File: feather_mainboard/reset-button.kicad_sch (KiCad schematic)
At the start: 4 parts

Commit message: changed footprints location to match the new folder. TODO: check if the path is working on another computer
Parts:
- C10: footprint footprints:WCAP-CSGP_1210_H2.0 -> Custom footprints:WCAP-CSGP_1210_H2.0
- S5: footprint footprints:430182050816 -> Custom footprints:430182050816
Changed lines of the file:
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@@
 			)
 		)
-		(property "Footprint" "footprints:WCAP-CSGP_1210_H2.0"
+		(property "Footprint" "Custom footprints:WCAP-CSGP_1210_H2.0"
 			(at 125.73 106.68 0)
 			(effects
@@
 			)
 		)
-		(property "Footprint" "footprints:430182050816"
+		(property "Footprint" "Custom footprints:430182050816"
 			(at 147.32 106.68 0)
 			(effects

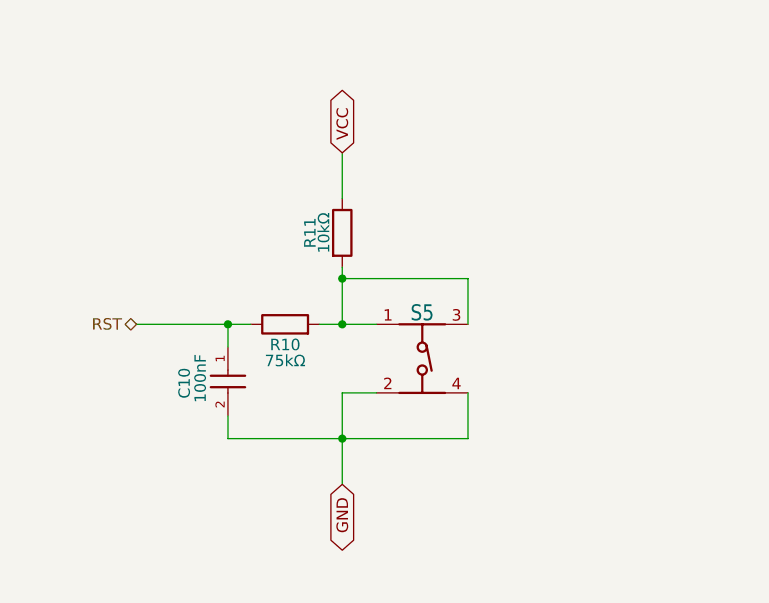
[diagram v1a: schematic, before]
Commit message: added daughter board
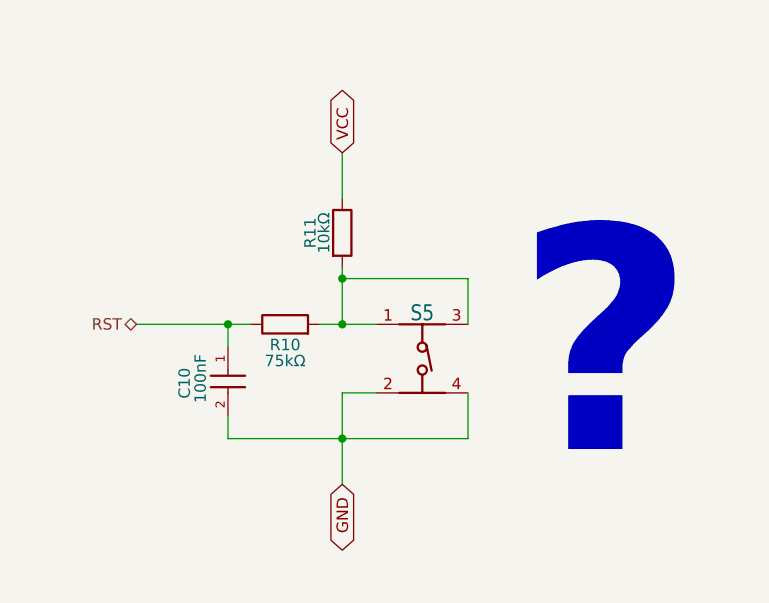
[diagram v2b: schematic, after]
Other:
- note added: "?"
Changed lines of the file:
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@@
+		)
+	)
+	(text "?"
+		(exclude_from_sim no)
+		(at 167.64 104.14 0)
+		(effects
+			(font
+				(size 25 25)
+				(thickness 5)
+				(bold yes)
+			)
 		)
 	)

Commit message: finished mainboard design, need to do the routing
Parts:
- removed C10: 100nF, Custom footprints:WCAP-CSGP_1210_H2.0, symbol WCAP-CSGP_1210_H2.0:WCAP-CSGP_1210_H2.0
- removed R10: 75kΩ, Resistor_SMD:R_0805_2012Metric_Pad1.20x1.40mm_HandSolder, symbol Device:R
- removed R11: 10kΩ, Resistor_SMD:R_0805_2012Metric_Pad1.20x1.40mm_HandSolder, symbol Device:R
- removed S5: 430182050816, Custom footprints:430182050816, symbol Projektarbeit_button:430182050816
- added C1_3: 100nF, Custom footprints:WCAP-CSGP_0603_R, symbol WCAP-CSGP_0603:WCAP-CSGP_0603
- added J3: 61300211121, Custom footprints:61300211121, symbol 6130XX11121_61300211121:6130XX11121_61300211121
- added R1_5: 10kΩ, Custom footprints:WRIS-RSKS_0603_REFLOW, symbol WRIS-RSKS_0603:WRIS-RSKS_0603
- added R3_1: 75kΩ, Custom footprints:WRIS-RSKS_0603_REFLOW, symbol WRIS-RSKS_0603:WRIS-RSKS_0603
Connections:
- net GND: now also C1_3.2, J3.2
- net RST: now also C1_3.1, R3_1.1
- net VCC: now also R1_5.2
- new net: J3.1, R1_5.1, R3_1.2
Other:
- note removed: "?"

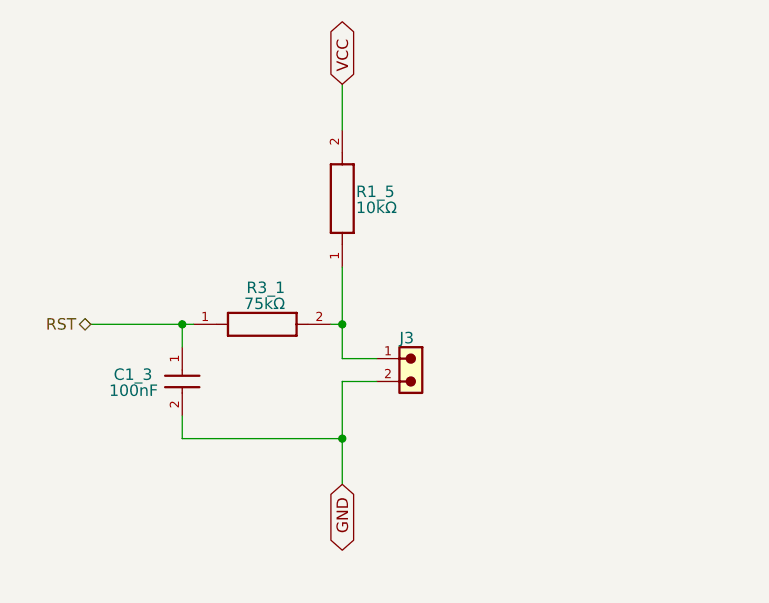
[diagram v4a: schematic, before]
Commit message: Updated the mainboard: removed unnecessary pull-ups on SD card lines; connected IIC pull-ups to enable circuit; cleaned up schematic
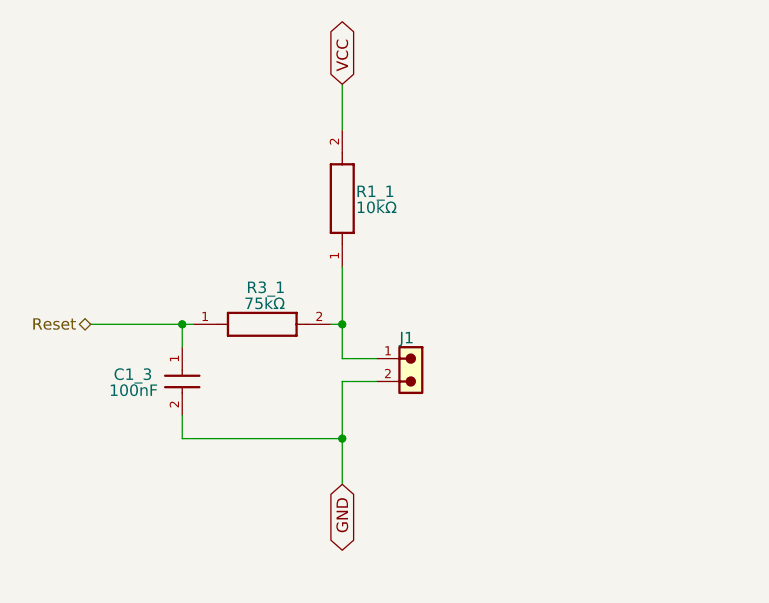
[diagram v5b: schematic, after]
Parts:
- renumbered J3 to J1, R1_5 to R1_1
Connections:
- net RST renamed Reset
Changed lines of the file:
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@@
 		)
 	)
-	(hierarchical_label "RST"
+	(hierarchical_label "Reset"
 		(shape bidirectional)
 		(at 110.49 101.6 180)
+		(fields_autoplaced yes)
 		(effects
 			(font
@@
 		(instances
 			(project "feather_mainboard"
-				(path "/e1e12730-ab4f-45db-8b66-c1e0f78e2f00/0d3ffa4d-b734-4a21-ae0e-364ca9762bbd"
+				(path "/e1e12730-ab4f-45db-8b66-c1e0f78e2f00/05fa08fc-e98a-44c0-b5db-55a9f347530b"
 					(reference "C1_3")
 					(unit 1)
@@
 		(on_board yes)
 		(dnp no)
-		(property "Reference" "J3"
+		(property "Reference" "J1"
 			(at 144.78 103.124 90)
 			(effects
@@
 		(instances
 			(project "feather_mainboard"
-				(path "/e1e12730-ab4f-45db-8b66-c1e0f78e2f00/0d3ffa4d-b734-4a21-ae0e-364ca9762bbd"
-					(reference "J3")
+				(path "/e1e12730-ab4f-45db-8b66-c1e0f78e2f00/05fa08fc-e98a-44c0-b5db-55a9f347530b"
+					(reference "J1")
 					(unit 1)
 				)
@@
 		(on_board yes)
 		(dnp no)
-		(property "Reference" "R1_5"
+		(property "Reference" "R1_1"
 			(at 139.954 86.868 90)
 			(effects
@@
 		(instances
 			(project "feather_mainboard"
-				(path "/e1e12730-ab4f-45db-8b66-c1e0f78e2f00/0d3ffa4d-b734-4a21-ae0e-364ca9762bbd"
-					(reference "R1_5")
+				(path "/e1e12730-ab4f-45db-8b66-c1e0f78e2f00/05fa08fc-e98a-44c0-b5db-55a9f347530b"
+					(reference "R1_1")
 					(unit 1)
 				)
@@
 		(instances
 			(project "feather_mainboard"
-				(path "/e1e12730-ab4f-45db-8b66-c1e0f78e2f00/0d3ffa4d-b734-4a21-ae0e-364ca9762bbd"
+				(path "/e1e12730-ab4f-45db-8b66-c1e0f78e2f00/05fa08fc-e98a-44c0-b5db-55a9f347530b"
 					(reference "R3_1")
 					(unit 1)
